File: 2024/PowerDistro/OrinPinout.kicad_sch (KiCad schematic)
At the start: 1 part

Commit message: save something
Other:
- note added: "Orin Pinout"
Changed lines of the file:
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@@
 	(paper "A4")
 	(junction
-		(at 191.77 101.6)
+		(at 187.96 101.6)
 		(diameter 0)
 		(color 0 0 0 0)
@@
 	)
 	(junction
-		(at 191.77 114.3)
+		(at 187.96 114.3)
 		(diameter 0)
 		(color 0 0 0 0)
@@
 	)
 	(junction
-		(at 191.77 93.98)
+		(at 187.96 93.98)
 		(diameter 0)
 		(color 0 0 0 0)
@@
 	)
 	(junction
-		(at 191.77 119.38)
-		(diameter 0)
-		(color 0 0 0 0)
-	)
-	(wire
-		(pts
-			(xy 191.77 138.43) (xy 140.97 138.43)
+		(at 187.96 119.38)
+		(diameter 0)
+		(color 0 0 0 0)
+	)
+	(wire
+		(pts
+			(xy 187.96 138.43) (xy 140.97 138.43)
 		)
 		(stroke
@@
 	(wire
 		(pts
-			(xy 191.77 93.98) (xy 191.77 101.6)
+			(xy 187.96 93.98) (xy 187.96 101.6)
 		)
 		(stroke
@@
 	(wire
 		(pts
-			(xy 191.77 83.82) (xy 191.77 93.98)
-		)
-		(stroke
-			(width 0)
-			(type default)
-		)
-	)
-	(wire
-		(pts
-			(xy 191.77 119.38) (xy 191.77 138.43)
+			(xy 187.96 83.82) (xy 187.96 93.98)
+		)
+		(stroke
+			(width 0)
+			(type default)
+		)
+	)
+	(wire
+		(pts
+			(xy 187.96 119.38) (xy 187.96 138.43)
 		)
 		(stroke
@@
 	(wire
 		(pts
-			(xy 191.77 101.6) (xy 191.77 114.3)
+			(xy 187.96 101.6) (xy 187.96 114.3)
 		)
 		(stroke
@@
 	(wire
 		(pts
-			(xy 157.48 93.98) (xy 191.77 93.98)
-		)
-		(stroke
-			(width 0)
-			(type default)
-		)
-	)
-	(wire
-		(pts
-			(xy 157.48 101.6) (xy 191.77 101.6)
-		)
-		(stroke
-			(width 0)
-			(type default)
-		)
-	)
-	(wire
-		(pts
-			(xy 157.48 119.38) (xy 191.77 119.38)
+			(xy 157.48 93.98) (xy 187.96 93.98)
+		)
+		(stroke
+			(width 0)
+			(type default)
+		)
+	)
+	(wire
+		(pts
+			(xy 157.48 101.6) (xy 187.96 101.6)
+		)
+		(stroke
+			(width 0)
+			(type default)
+		)
+	)
+	(wire
+		(pts
+			(xy 157.48 119.38) (xy 187.96 119.38)
 		)
 		(stroke
@@
 	(wire
 		(pts
-			(xy 157.48 83.82) (xy 191.77 83.82)
+			(xy 157.48 83.82) (xy 187.96 83.82)
 		)
 		(stroke
@@
 	(wire
 		(pts
-			(xy 191.77 114.3) (xy 191.77 119.38)
-		)
-		(stroke
-			(width 0)
-			(type default)
-		)
-	)
-	(wire
-		(pts
-			(xy 157.48 114.3) (xy 191.77 114.3)
-		)
-		(stroke
-			(width 0)
-			(type default)
-		)
-	)
+			(xy 187.96 114.3) (xy 187.96 119.38)
+		)
+		(stroke
+			(width 0)
+			(type default)
+		)
+	)
+	(wire
+		(pts
+			(xy 157.48 114.3) (xy 187.96 114.3)
+		)
+		(stroke
+			(width 0)
+			(type default)
+		)
+	)
+	(text "Orin Pinout\n"
+		(exclude_from_sim no)
+		(at 140.97 67.31 0)
+		(effects
+			(font
+				(size 1.27 1.27)
+			)
+		)
+	)

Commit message: Added PCA 9862 to Power distro schematic and started PCB
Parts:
- J9: footprint (none) -> Connector_PinHeader_2.54mm:PinHeader_2x20_P2.54mm_Vertical_SMD
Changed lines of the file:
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@@
 			)
 		)
-		(property "Footprint" ""
+		(property "Footprint" "Connector_PinHeader_2.54mm:PinHeader_2x20_P2.54mm_Vertical_SMD"
 			(at 139.7 72.39 0)
 			(effects

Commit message: Added EASYBldc Outlines
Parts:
- added H1: MountingHole, symbol Mechanical:MountingHole
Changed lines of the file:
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@@
+		)
+	)
+	(symbol
+		(lib_id "Mechanical:MountingHole")
+		(at 26.67 29.21 0)
+		(unit 1)
+		(exclude_from_sim yes)
+		(in_bom no)
+		(on_board yes)
+		(dnp no)
+		(fields_autoplaced yes)
+		(property "Reference" "H1"
+			(at 29.21 27.9399 0)
+			(effects
+				(font
+					(size 1.27 1.27)
+				)
+				(justify left)
+			)
+		)
+		(property "Value" "MountingHole"
+			(at 29.21 30.4799 0)
+			(effects
+				(font
+					(size 1.27 1.27)
+				)
+				(justify left)
+			)
+		)
+		(property "Footprint" ""
+			(at 26.67 29.21 0)
+			(effects
+				(font
+					(size 1.27 1.27)
+				)
+				(hide yes)
+			)
+		)
+		(property "Datasheet" "~"
+			(at 26.67 29.21 0)
+			(effects
+				(font
+					(size 1.27 1.27)
+				)
+				(hide yes)
+			)
+		)
+		(property "Description" "Mounting Hole without connection"
+			(at 26.67 29.21 0)
+			(effects
+				(font
+					(size 1.27 1.27)
+				)
+				(hide yes)
+			)
+		)
+		(instances
+			(project ""
+				(path "/605eff46-b281-4cd5-84ac-aa97178bb7be/487f4da6-9a33-4c8e-8a5a-04392d82f5a1"
+					(reference "H1")
+					(unit 1)
+				)
+			)
 		)
 	)

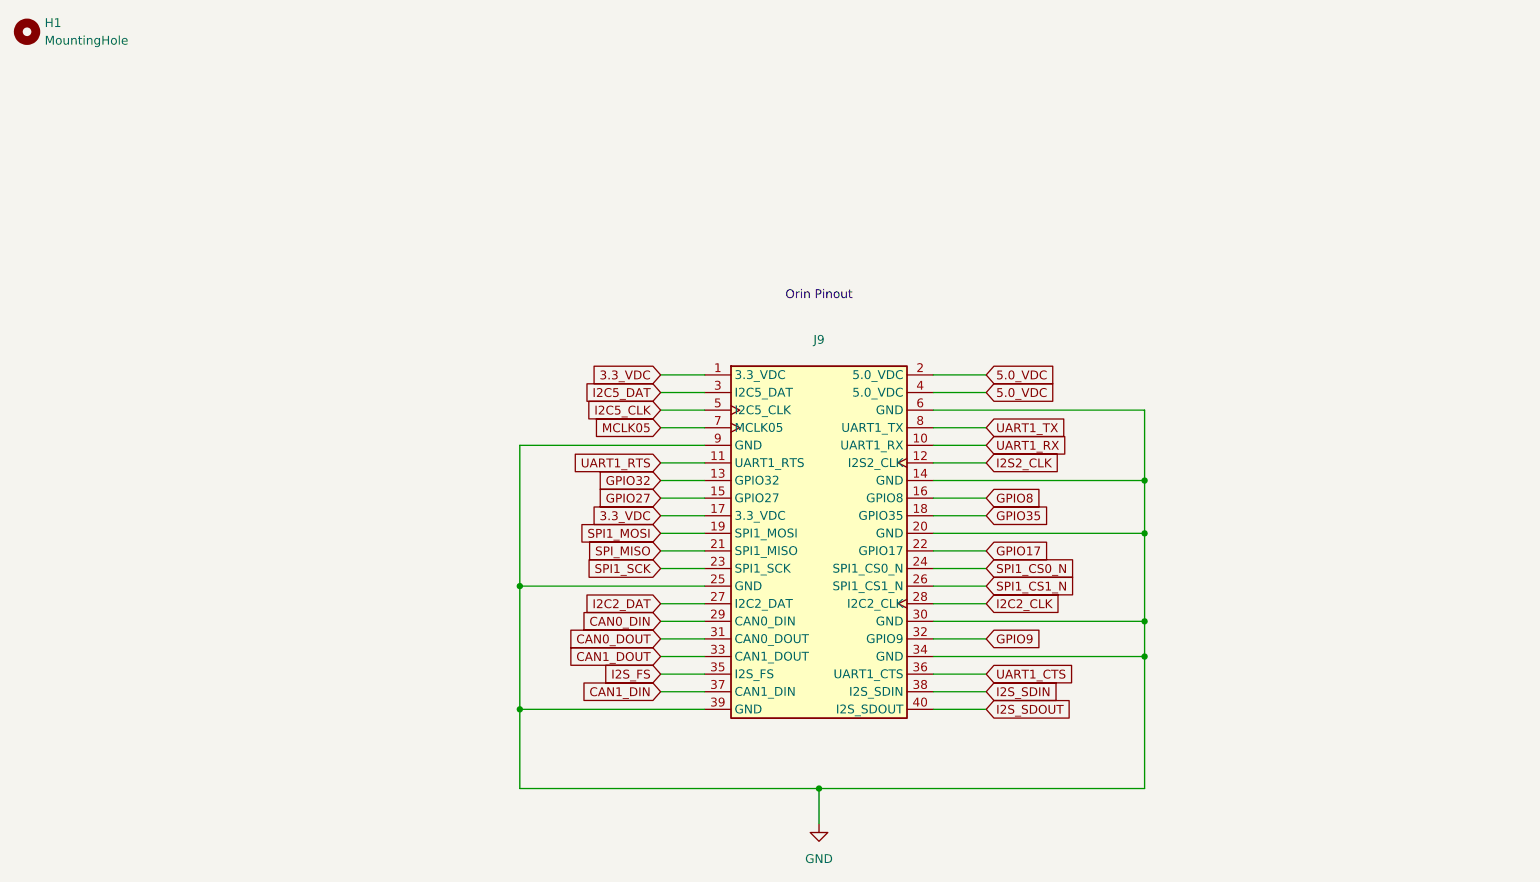
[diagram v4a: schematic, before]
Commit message: Added connectors and esc footprints
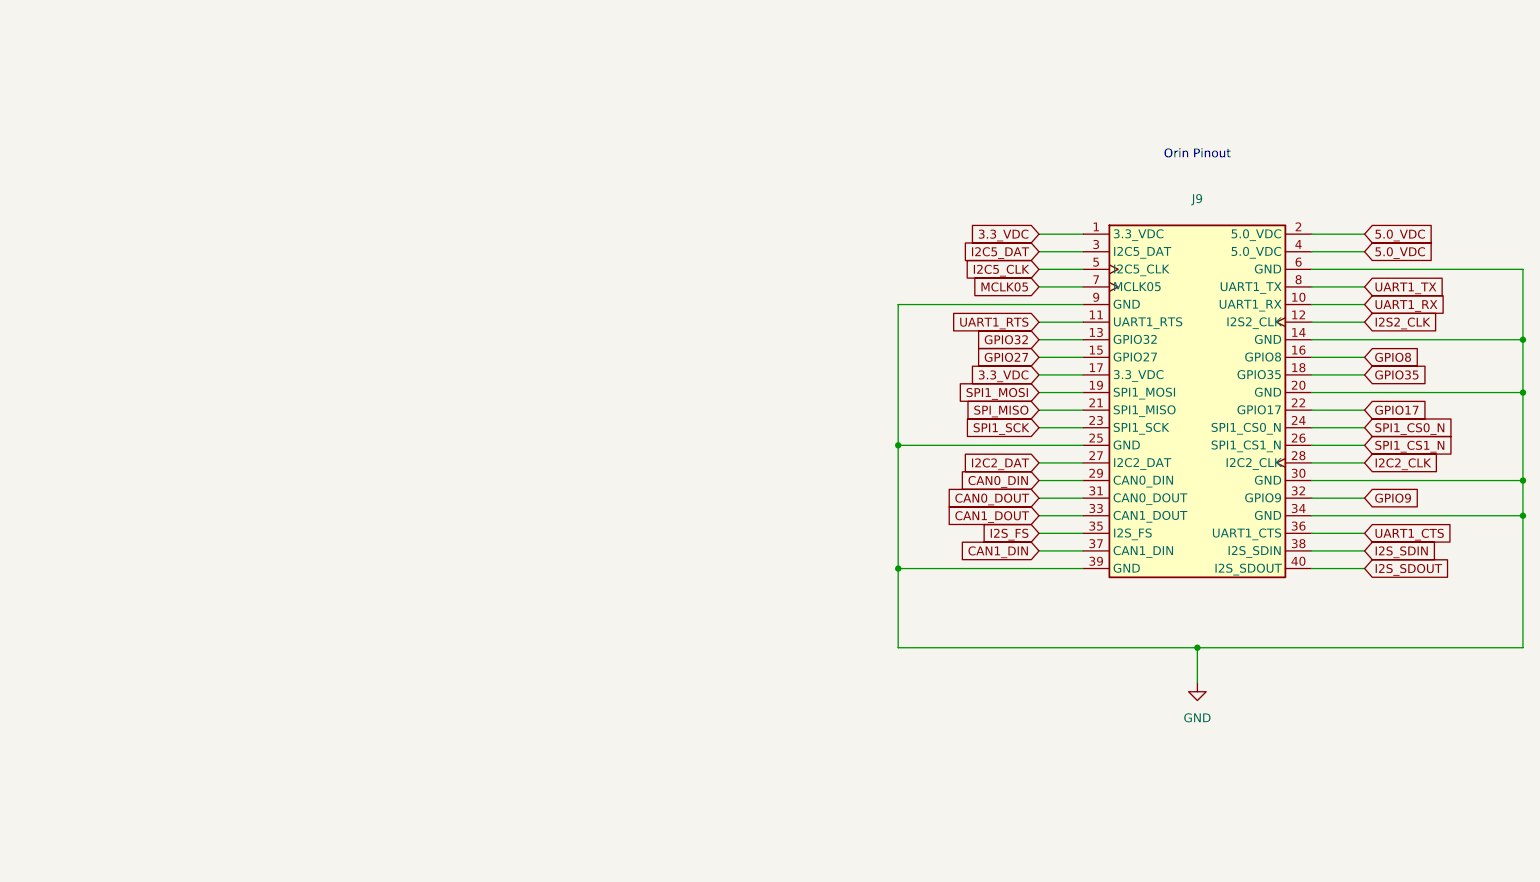
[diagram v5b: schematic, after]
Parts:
- removed H1: MountingHole, symbol Mechanical:MountingHole
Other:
- moved on the sheet: J9

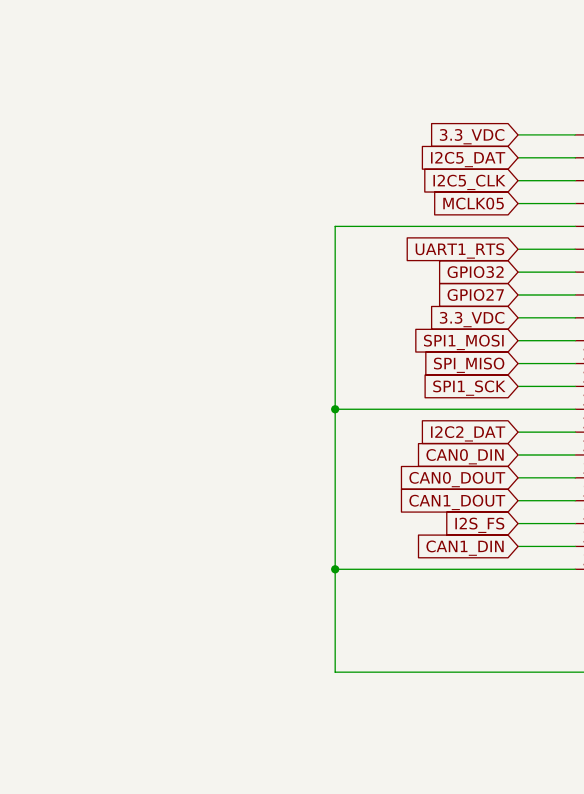
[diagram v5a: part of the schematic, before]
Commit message: Added power layer to power distro motors
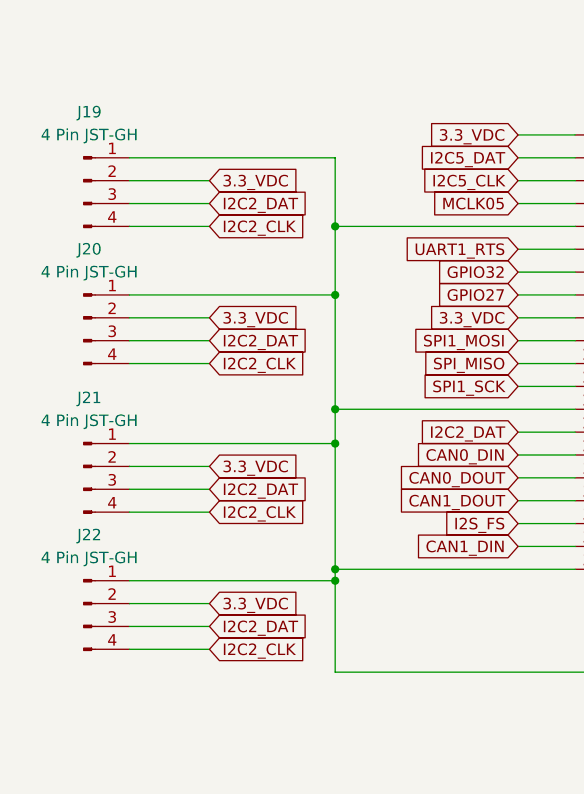
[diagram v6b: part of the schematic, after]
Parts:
- added J19, J20, J21, J22: 4 Pin JST-GH, PowerDistroFootprints:JST_BM04B-GHS-TBT_LF__SN__N_, symbol Connector:Conn_01x04_Pin
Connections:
- net 3.3_VDC: now also J19.2 (Pin_2), J20.2 (Pin_2), J21.2 (Pin_2), J22.2 (Pin_2)
- net GND: now also J19.1 (Pin_1), J20.1 (Pin_1), J21.1 (Pin_1), J22.1 (Pin_1)
- net I2C2_CLK: now also J19.4 (Pin_4), J20.4 (Pin_4), J21.4 (Pin_4), J22.4 (Pin_4)
- net I2C2_DAT: now also J19.3 (Pin_3), J20.3 (Pin_3), J21.3 (Pin_3), J22.3 (Pin_3)

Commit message: Changed Everything
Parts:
- removed J9: ~, Connector_PinHeader_2.54mm:PinHeader_2x20_P2.54mm_Vertical_SMD, symbol PowerDistro:JetsonAGXOrinExpansionHeader
- added J9: Conn_01x05_Pin, Connector_PinHeader_2.54mm:PinHeader_1x05_P2.54mm_Vertical, symbol Connector:Conn_01x05_Pin
- J19, J20, J21, J22: footprint PowerDistroFootprints:JST_BM04B-GHS-TBT_LF__SN__N_ -> Connector_JST:JST_XH_B4B-XH-A_1x04_P2.50mm_Vertical
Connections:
- net 3.3_VDC: now also J9.1 (Pin_1)
- net GND: now also J9.5 (Pin_5)
- net I2C5_CLK: now also J9.3 (Pin_3)
- net I2C5_DAT: now also J9.2 (Pin_2)
- net MCLK05: now also J9.4 (Pin_4)
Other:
- note added: "Aux Connectors"
- moved on the sheet: J19, J20, J21, J22

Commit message: Release
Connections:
- net I2C5_CLK is gone; now on net I2C_CLK: J9.3 (Pin_3)
- net I2C5_DAT is gone; now on net I2C_DAT: J9.2 (Pin_2)
- net I2C2_CLK renamed I2C_CLK
- net I2C2_DAT renamed I2C_DAT
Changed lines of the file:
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@@
 		)
 	)
-	(global_label "I2C2_DAT"
+	(global_label "I2C_DAT"
 		(shape input)
 		(at 139.7 93.98 0)
@@
 		)
 		(property "Intersheetrefs" "${INTERSHEET_REFS}"
-			(at 151.2728 93.98 0)
+			(at 150.0633 93.98 0)
 			(effects
 				(font
@@
 		)
 	)
-	(global_label "I2C2_DAT"
+	(global_label "I2C_DAT"
 		(shape input)
 		(at 139.7 77.47 0)
@@
 		)
 		(property "Intersheetrefs" "${INTERSHEET_REFS}"
-			(at 151.2728 77.47 0)
-			(effects
-				(font
-					(size 1.27 1.27)
-				)
-				(justify left)
-				(hide yes)
-			)
-		)
-	)
-	(global_label "I2C2_CLK"
+			(at 150.0633 77.47 0)
+			(effects
+				(font
+					(size 1.27 1.27)
+				)
+				(justify left)
+				(hide yes)
+			)
+		)
+	)
+	(global_label "I2C_CLK"
 		(shape input)
 		(at 139.7 57.15 0)
@@
 		)
 		(property "Intersheetrefs" "${INTERSHEET_REFS}"
-			(at 151.5147 57.15 0)
-			(effects
-				(font
-					(size 1.27 1.27)
-				)
-				(justify left)
-				(hide yes)
-			)
-		)
-	)
-	(global_label "I2C2_CLK"
+			(at 150.3052 57.15 0)
+			(effects
+				(font
+					(size 1.27 1.27)
+				)
+				(justify left)
+				(hide yes)
+			)
+		)
+	)
+	(global_label "I2C_CLK"
 		(shape input)
 		(at 139.7 74.93 0)
@@
 		)
 		(property "Intersheetrefs" "${INTERSHEET_REFS}"
-			(at 151.5147 74.93 0)
+			(at 150.3052 74.93 0)
 			(effects
 				(font
@@
 		)
 	)
-	(global_label "I2C5_DAT"
+	(global_label "I2C_DAT"
 		(shape input)
 		(at 213.36 62.23 0)
@@
 		)
 		(property "Intersheetrefs" "${INTERSHEET_REFS}"
-			(at 224.9328 62.23 0)
+			(at 223.7233 62.23 0)
 			(effects
 				(font
@@
 		)
 	)
-	(global_label "I2C2_CLK"
+	(global_label "I2C_CLK"
 		(shape input)
 		(at 139.7 91.44 0)
@@
 		)
 		(property "Intersheetrefs" "${INTERSHEET_REFS}"
-			(at 151.5147 91.44 0)
-			(effects
-				(font
-					(size 1.27 1.27)
-				)
-				(justify left)
-				(hide yes)
-			)
-		)
-	)
-	(global_label "I2C2_DAT"
+			(at 150.3052 91.44 0)
+			(effects
+				(font
+					(size 1.27 1.27)
+				)
+				(justify left)
+				(hide yes)
+			)
+		)
+	)
+	(global_label "I2C_DAT"
 		(shape input)
 		(at 139.7 59.69 0)
@@
 		)
 		(property "Intersheetrefs" "${INTERSHEET_REFS}"
-			(at 151.2728 59.69 0)
+			(at 150.0633 59.69 0)
 			(effects
 				(font
@@
 		)
 	)
-	(global_label "I2C2_CLK"
+	(global_label "I2C_CLK"
 		(shape input)
 		(at 139.7 109.22 0)
@@
 		)
 		(property "Intersheetrefs" "${INTERSHEET_REFS}"
-			(at 151.5147 109.22 0)
-			(effects
-				(font
-					(size 1.27 1.27)
-				)
-				(justify left)
-				(hide yes)
-			)
-		)
-	)
-	(global_label "I2C2_DAT"
+			(at 150.3052 109.22 0)
+			(effects
+				(font
+					(size 1.27 1.27)
+				)
+				(justify left)
+				(hide yes)
+			)
+		)
+	)
+	(global_label "I2C_DAT"
 		(shape input)
 		(at 139.7 111.76 0)
@@
 		)
 		(property "Intersheetrefs" "${INTERSHEET_REFS}"
-			(at 151.2728 111.76 0)
-			(effects
-				(font
-					(size 1.27 1.27)
-				)
-				(justify left)
-				(hide yes)
-			)
-		)
-	)
-	(global_label "I2C5_CLK"
+			(at 150.0633 111.76 0)
+			(effects
+				(font
+					(size 1.27 1.27)
+				)
+				(justify left)
+				(hide yes)
+			)
+		)
+	)
+	(global_label "I2C_CLK"
 		(shape input)
 		(at 213.36 64.77 0)
@@
 		)
 		(property "Intersheetrefs" "${INTERSHEET_REFS}"
-			(at 225.1747 64.77 0)
-			(effects
-				(font
+			(at 223.9652 64.77 0)
+			(effects
+				(font
